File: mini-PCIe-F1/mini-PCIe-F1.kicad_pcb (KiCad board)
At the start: 2 copper layers, 50.9 x 30 mm, 2 parts

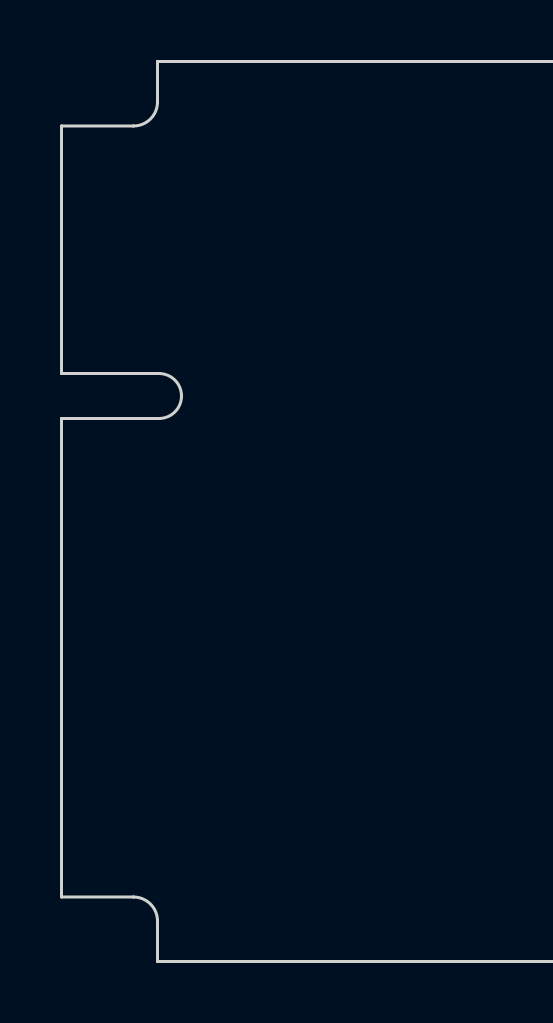
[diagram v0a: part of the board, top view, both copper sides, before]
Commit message: Fixes connector placement in F1 template
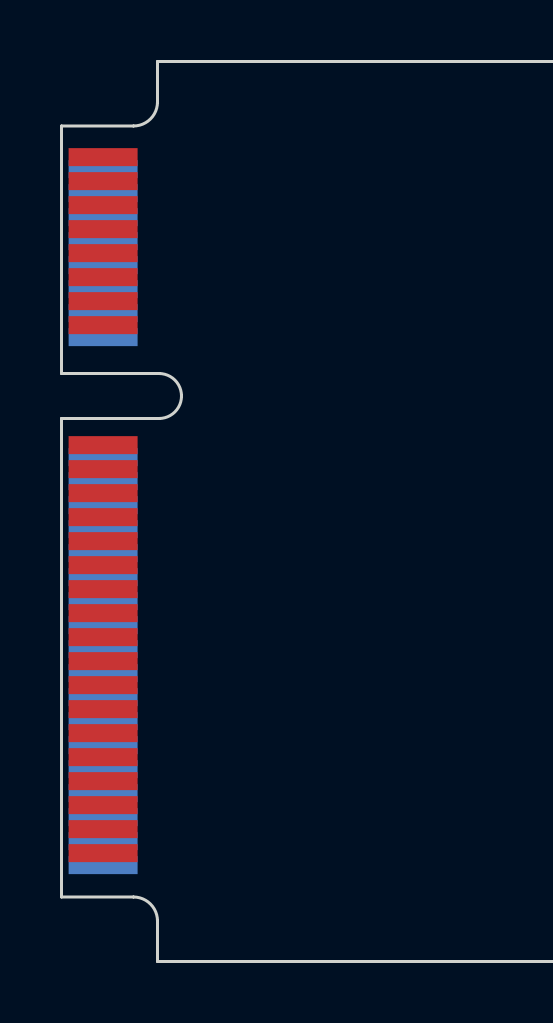
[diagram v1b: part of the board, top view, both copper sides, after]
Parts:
- added J1: PCIE-MINI, mini-PCIe:miniPCIeConn, F.Cu at (116.5, 61.6)
